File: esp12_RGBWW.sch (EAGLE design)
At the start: 21 parts

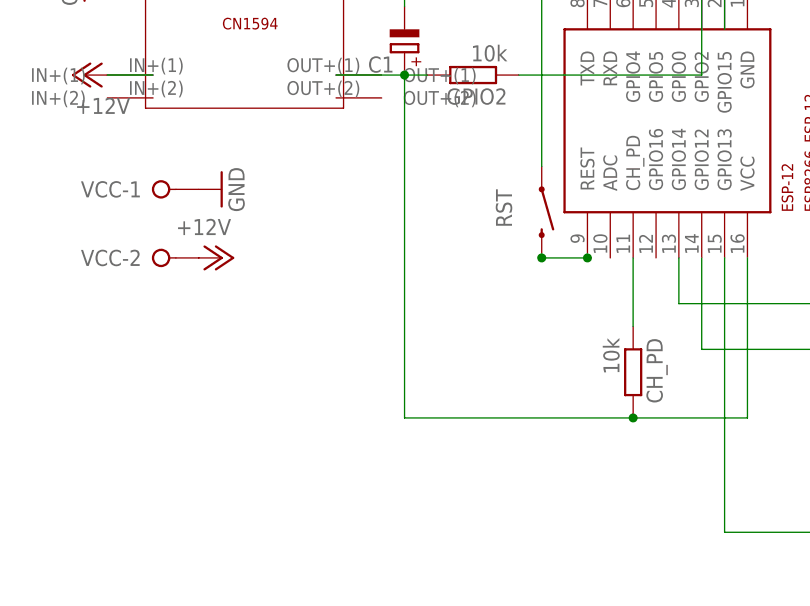
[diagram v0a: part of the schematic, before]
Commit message: added ADC and updated board layout
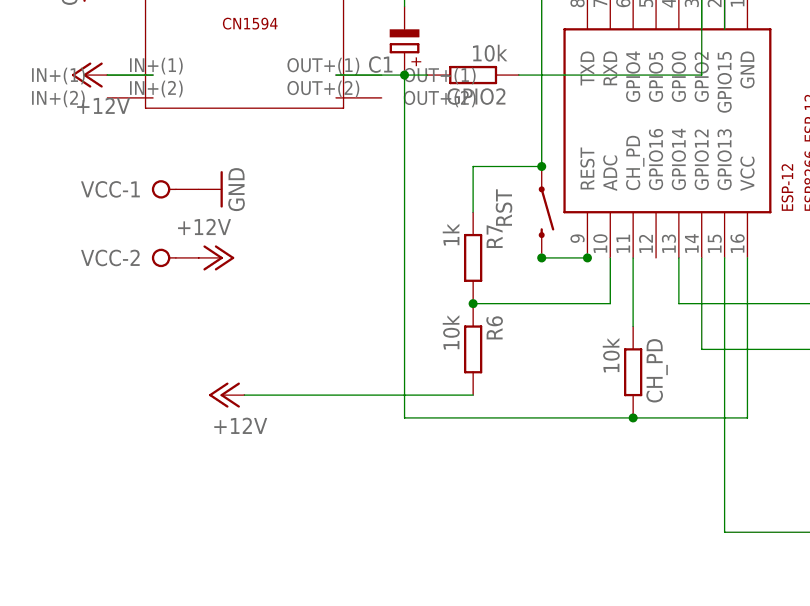
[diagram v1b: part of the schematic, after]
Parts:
- added R6: 10k, rcl:R-EU_R0805
- added R7: 1k, rcl:R-EU_R0805
- CH_PD, GPIO15, GPIO2, R1, R2, R3, R4, R5: device rcl:R-EU_R0603 -> rcl:R-EU_R0805
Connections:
- new net N$21: ESP-12.ADC, R6.1, R7.2
- net +12V: now also R6.2
- net GND3.3V: now also R7.1
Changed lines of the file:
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@@
 <class number="0" name="default" width="0" drill="0">
 </class>
-<class number="1" name="12V" width="1.016" drill="0">
-</class>
-<class number="2" name="GNDRGB" width="1.016" drill="0">
-</class>
-<class number="3" name="3.3V" width="0.635" drill="0">
-</class>
-<class number="4" name="GND3.3V" width="0.635" drill="0">
+<class number="1" name="12V" width="0.508" drill="0">
+</class>
+<class number="2" name="GNDRGB" width="0.508" drill="0">
+</class>
+<class number="3" name="3.3V" width="0.508" drill="0">
+</class>
+<class number="4" name="GND3.3V" width="0.508" drill="0">
 </class>
 <class number="5" name="Signal" width="0.381" drill="0">
@@
 </classes>
 <parts>
-<part name="GPIO2" library="rcl" deviceset="R-EU_" device="R0603" value="10k"/>
-<part name="GPIO15" library="rcl" deviceset="R-EU_" device="R0603" value="10k"/>
-<part name="CH_PD" library="rcl" deviceset="R-EU_" device="R0603" value="10k"/>
+<part name="GPIO2" library="rcl" deviceset="R-EU_" device="R0805" value="10k"/>
+<part name="GPIO15" library="rcl" deviceset="R-EU_" device="R0805" value="10k"/>
+<part name="CH_PD" library="rcl" deviceset="R-EU_" device="R0805" value="10k"/>
 <part name="DC_CONVERTER" library="CN1594_smd" deviceset="CN1594" device="THROUGH-HOLE"/>
 <part name="ESP-12" library="ESP8266-ESP12" deviceset="ESP8266_ESP-12" device=""/>
-<part name="R1" library="rcl" deviceset="R-EU_" device="R0603" value="10k"/>
-<part name="R3" library="rcl" deviceset="R-EU_" device="R0603" value="10k"/>
-<part name="R2" library="rcl" deviceset="R-EU_" device="R0603" value="10k"/>
+<part name="R1" library="rcl" deviceset="R-EU_" device="R0805" value="10k"/>
+<part name="R3" library="rcl" deviceset="R-EU_" device="R0805" value="10k"/>
+<part name="R2" library="rcl" deviceset="R-EU_" device="R0805" value="10k"/>
 <part name="IRLZ44N-WW" library="PAsystem" deviceset="TIP121" device="" value=""/>
 <part name="IRLZ44N-CW" library="PAsystem" deviceset="TIP121" device="" value=""/>
@@
 <part name="IRLZ44N-G" library="PAsystem" deviceset="TIP121" device="" value=""/>
 <part name="IRLZ44N-R" library="PAsystem" deviceset="TIP121" device="" value=""/>
-<part name="R4" library="rcl" deviceset="R-EU_" device="R0603" value="10k"/>
-<part name="R5" library="rcl" deviceset="R-EU_" device="R0603" value="10k"/>
+<part name="R4" library="rcl" deviceset="R-EU_" device="R0805" value="10k"/>
+<part name="R5" library="rcl" deviceset="R-EU_" device="R0805" value="10k"/>
 <part name="P+1" library="supply1" deviceset="+12V" device=""/>
 <part name="P+2" library="supply1" deviceset="+12V" device=""/>
@@
 <part name="RGB" library="con-wago-508" deviceset="W237-04P" device=""/>
 <part name="C1" library="rcl" deviceset="CPOL-EU" device="E3.5-8"/>
+<part name="P+5" library="supply1" deviceset="+12V" device=""/>
+<part name="R6" library="rcl" deviceset="R-EU_" device="R0805" value="10k"/>
+<part name="R7" library="rcl" deviceset="R-EU_" device="R0805" value="1k"/>
 </parts>
 <sheets>
@@
 <instance part="RGB" gate="-4" x="63.5" y="20.32" rot="R180"/>
 <instance part="C1" gate="G$1" x="-48.26" y="53.34" rot="R180"/>
+<instance part="P+5" gate="1" x="-68.58" y="15.24" rot="R90"/>
+<instance part="R6" gate="G$1" x="-40.64" y="20.32" rot="R270"/>
+<instance part="R7" gate="G$1" x="-40.64" y="30.48" rot="R270"/>
 </instances>
 <busses>
@@
 </segment>
 </net>
-<net name="GND" class="2">
+<net name="GND" class="0">
 <segment>
 <pinref part="IRLZ44N-WW" gate="G$1" pin="E"/>
@@
 </segment>
 </net>
-<net name="N$11" class="2">
+<net name="N$11" class="0">
 <segment>
 <pinref part="IRLZ44N-B" gate="G$1" pin="C"/>
@@
 <junction x="-48.26" y="60.96"/>
 <junction x="-10.16" y="76.2"/>
+<wire x1="-40.64" y1="40.64" x2="-33.02" y2="40.64" width="0.1524" layer="91"/>
+<junction x="-33.02" y="40.64"/>
+<pinref part="R7" gate="G$1" pin="1"/>
+<wire x1="-40.64" y1="35.56" x2="-40.64" y2="40.64" width="0.1524" layer="91"/>
 </segment>
 </net>
@@
 <wire x1="-45.72" y1="50.8" x2="-48.26" y2="50.8" width="0.1524" layer="91"/>
 <wire x1="-48.26" y1="50.8" x2="-48.26" y2="12.7" width="0.1524" layer="91"/>
+<junction x="-22.86" y="12.7"/>
 <wire x1="-48.26" y1="12.7" x2="-22.86" y2="12.7" width="0.1524" layer="91"/>
-<junction x="-22.86" y="12.7"/>
 <wire x1="-22.86" y1="12.7" x2="-10.16" y2="12.7" width="0.1524" layer="91"/>
 <wire x1="-55.88" y1="50.8" x2="-48.26" y2="50.8" width="0.1524" layer="91"/>
@@
 <wire x1="-81.28" y1="50.8" x2="-76.2" y2="50.8" width="0.1524" layer="91"/>
 </segment>
+<segment>
+<pinref part="R6" gate="G$1" pin="2"/>
+<pinref part="P+5" gate="1" pin="+12V"/>
+<wire x1="-66.04" y1="15.24" x2="-40.64" y2="15.24" width="0.1524" layer="91"/>
+</segment>
 </net>
 <net name="N$10" class="0">
@@
 </segment>
 </net>
+<net name="N$21" class="4">
+<segment>
+<pinref part="ESP-12" gate="G$1" pin="ADC"/>
+<pinref part="R6" gate="G$1" pin="1"/>
+<wire x1="-40.64" y1="25.4" x2="-25.4" y2="25.4" width="0.1524" layer="91"/>
+<wire x1="-25.4" y1="25.4" x2="-25.4" y2="30.48" width="0.1524" layer="91"/>
+<pinref part="R7" gate="G$1" pin="2"/>
+<junction x="-40.64" y="25.4"/>
+</segment>
+</net>

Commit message: v1.2
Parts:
- added C2: 100n, rcl:C-EUC0805
- added C3: (no value), resistor:CPOL-EUE2.5-6
- added REST: 10k, rcl:R-EU_R0805
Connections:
- removed net GND3.3V: C1.-, DC_CONVERTER.OUT-(2), ESP-12.GND, GPIO15.2, PROG.4, R1.1, R2.2, R3.2, R4.2, R5.2, R7.1, RST.1
- removed net N$20: C1.+, CH_PD.2, DC_CONVERTER.OUT+(1), ESP-12.VCC, GPIO2.2
- new net +3V3: C1.+, C2.2, CH_PD.2, DC_CONVERTER.OUT+(1), ESP-12.VCC, GPIO2.2, REST.1
- net +12V: now also C3.+
- net GND: now also C1.-, C2.1, C3.-, DC_CONVERTER.OUT-(2), ESP-12.GND, GPIO15.2, PROG.4, R1.1, R2.2, R3.2, R4.2, R5.2, R7.1, RST.1
- net N$12: now also REST.2
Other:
- moved on the sheet: C1, CH_PD, GPIO15, GPIO2, IRLZ44N-B, IRLZ44N-CW, IRLZ44N-G, IRLZ44N-R, IRLZ44N-WW, PROG, R1, R2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

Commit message: MOSFET netclass renamed
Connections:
- net N$10 renamed RGB-CW-OUT
- net N$11 renamed RGB-B-OUT
- net N$13 renamed RGB-B
- net N$15 renamed RGB-R-OUT
- net N$23 renamed RGB-R
- net N$24 renamed RGB-CW
- net N$25 renamed RGB-WW
- net N$4 renamed RGB-WW-OUT
- net N$6 renamed RGB-G-OUT
- net R4 renamed RGB-G
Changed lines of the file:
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@@
 </segment>
 </net>
-<net name="N$11" class="0">
+<net name="RGB-B-OUT" class="0">
 <segment>
 <pinref part="IRLZ44N-B" gate="G$1" pin="C"/>
@@
 </segment>
 </net>
-<net name="N$13" class="0">
+<net name="RGB-B" class="0">
 <segment>
 <wire x1="10.16" y1="15.24" x2="10.16" y2="0" width="0.1524" layer="91"/>
@@
 </segment>
 </net>
-<net name="R4" class="0">
+<net name="RGB-G" class="0">
 <segment>
 <wire x1="40.64" y1="20.32" x2="17.78" y2="20.32" width="0.1524" layer="91"/>
@@
 </segment>
 </net>
-<net name="N$15" class="0">
+<net name="RGB-R-OUT" class="0">
 <segment>
 <pinref part="IRLZ44N-R" gate="G$1" pin="C"/>
@@
 </segment>
 </net>
-<net name="N$10" class="0">
+<net name="RGB-CW-OUT" class="0">
 <segment>
 <pinref part="IRLZ44N-CW" gate="G$1" pin="C"/>
@@
 </segment>
 </net>
-<net name="N$6" class="0">
+<net name="RGB-G-OUT" class="0">
 <segment>
 <pinref part="RGB" gate="-3" pin="KL"/>
@@
 </segment>
 </net>
-<net name="N$4" class="0">
+<net name="RGB-WW-OUT" class="0">
 <segment>
 <pinref part="W" gate="-3" pin="KL"/>
@@
 </segment>
 </net>
-<net name="N$23" class="0">
+<net name="RGB-R" class="0">
 <segment>
 <pinref part="ESP-12" gate="G$1" pin="GPIO13"/>
@@
 </segment>
 </net>
-<net name="N$24" class="0">
+<net name="RGB-CW" class="0">
 <segment>
 <pinref part="ESP-12" gate="G$1" pin="GPIO5"/>
@@
 </segment>
 </net>
-<net name="N$25" class="5">
+<net name="RGB-WW" class="5">
 <segment>
 <pinref part="ESP-12" gate="G$1" pin="GPIO4"/>

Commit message: v1.3
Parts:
- added CLR: SWITCH-MOMENTARY-2SMD-1101NE, SparkFun-Electromechanical:SWITCH-MOMENTARY-2SMD-1101NE
- added R8: 10k, rcl:R-EU_R0805
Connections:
- new net N$1: CLR.2, ESP-12.GPIO16, R8.2
- net +3V3: now also R8.1
- net GND: now also CLR.1
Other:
- moved on the sheet: R6, R7, REST, RST

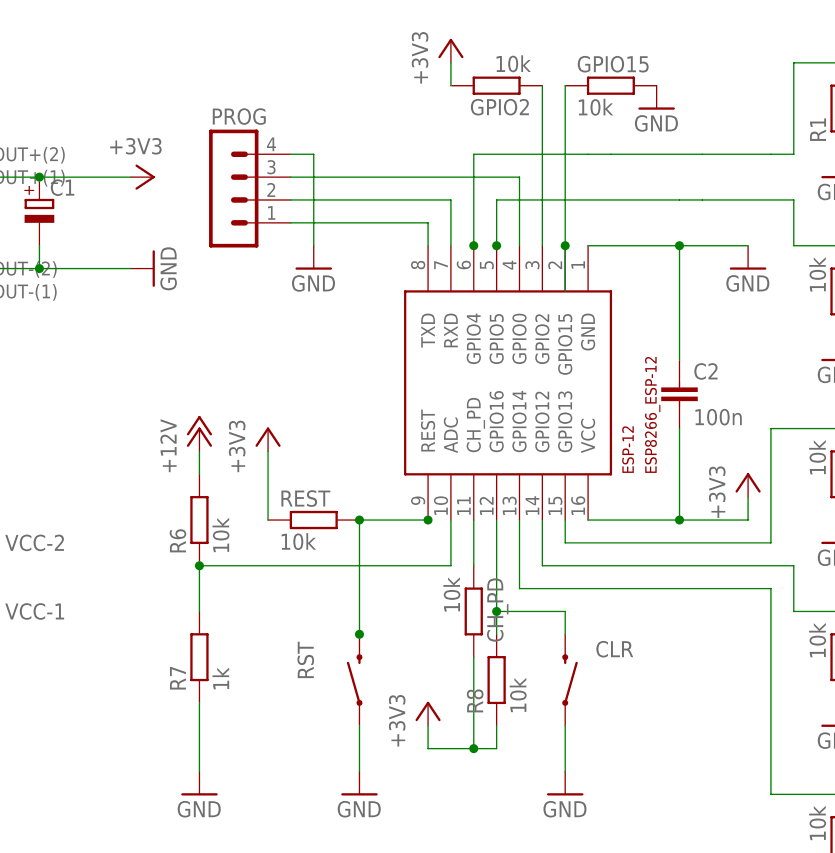
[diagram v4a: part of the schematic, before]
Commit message: updated silkscreen
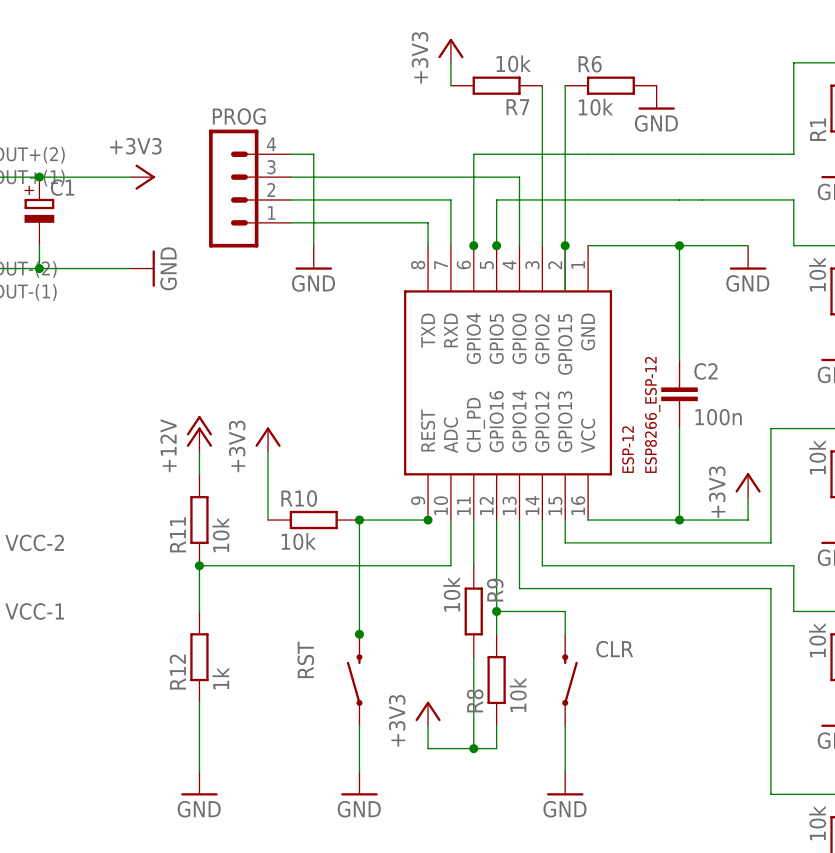
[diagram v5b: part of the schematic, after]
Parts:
- removed GPIO15, GPIO2: 10k, rcl:R-EU_R0805
- added R11: 10k, rcl:R-EU_R0805
- added R12: 1k, rcl:R-EU_R0805
- R7: value 1k -> 10k
- renumbered CH_PD to R9, REST to R10
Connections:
- net +12V: now also R11.2; no longer R6.2
- net +3V3: now also R7.2; no longer GPIO2.2
- net GND: now also R12.1, R6.2; no longer GPIO15.2, R7.1
- net N$21: now also R11.1, R12.2; no longer R6.1, R7.2
- net N$3: now also R7.1; no longer GPIO2.1
- net N$7: now also R6.1; no longer GPIO15.1
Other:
- moved on the sheet: R6, R7
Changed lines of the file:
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@@
 </classes>
 <parts>
-<part name="GPIO2" library="rcl" deviceset="R-EU_" device="R0805" value="10k"/>
-<part name="GPIO15" library="rcl" deviceset="R-EU_" device="R0805" value="10k"/>
-<part name="CH_PD" library="rcl" deviceset="R-EU_" device="R0805" value="10k"/>
+<part name="R7" library="rcl" deviceset="R-EU_" device="R0805" value="10k"/>
+<part name="R6" library="rcl" deviceset="R-EU_" device="R0805" value="10k"/>
+<part name="R9" library="rcl" deviceset="R-EU_" device="R0805" value="10k"/>
 <part name="DC_CONVERTER" library="CN1594_smd" deviceset="CN1594" device="THROUGH-HOLE"/>
 <part name="ESP-12" library="ESP8266-ESP12" deviceset="ESP8266_ESP-12" device=""/>
@@
 <part name="C1" library="rcl" deviceset="CPOL-EU" device="E3.5-8"/>
 <part name="P+5" library="supply1" deviceset="+12V" device=""/>
-<part name="R6" library="rcl" deviceset="R-EU_" device="R0805" value="10k"/>
-<part name="R7" library="rcl" deviceset="R-EU_" device="R0805" value="1k"/>
+<part name="R11" library="rcl" deviceset="R-EU_" device="R0805" value="10k"/>
+<part name="R12" library="rcl" deviceset="R-EU_" device="R0805" value="1k"/>
 <part name="+3V1" library="supply1" deviceset="+3V3" device=""/>
 <part name="+3V2" library="supply1" deviceset="+3V3" device=""/>
@@
 <part name="+3V4" library="supply1" deviceset="+3V3" device=""/>
 <part name="GND13" library="supply1" deviceset="GND" device=""/>
-<part name="REST" library="rcl" deviceset="R-EU_" device="R0805" value="10k"/>
+<part name="R10" library="rcl" deviceset="R-EU_" device="R0805" value="10k"/>
 <part name="+3V5" library="supply1" deviceset="+3V3" device=""/>
 <part name="C2" library="rcl" deviceset="C-EU" device="C0805" value="100n"/>
@@
 </plain>
 <instances>
-<instance part="GPIO2" gate="G$1" x="-20.32" y="78.74" rot="R180"/>
-<instance part="GPIO15" gate="G$1" x="-7.62" y="78.74"/>
-<instance part="CH_PD" gate="G$1" x="-22.86" y="20.32" rot="R270"/>
+<instance part="R7" gate="G$1" x="-20.32" y="78.74" rot="R180"/>
+<instance part="R6" gate="G$1" x="-7.62" y="78.74"/>
+<instance part="R9" gate="G$1" x="-22.86" y="20.32" rot="R270"/>
 <instance part="DC_CONVERTER" gate="G$1" x="-93.98" y="63.5" smashed="yes" rot="MR180"/>
 <instance part="ESP-12" gate="G$1" x="-20.32" y="53.34" rot="R90"/>
@@
 <instance part="C1" gate="G$1" x="-71.12" y="66.04"/>
 <instance part="P+5" gate="1" x="-53.34" y="40.64"/>
-<instance part="R6" gate="G$1" x="-53.34" y="30.48" rot="R90"/>
-<instance part="R7" gate="G$1" x="-53.34" y="15.24" rot="R90"/>
+<instance part="R11" gate="G$1" x="-53.34" y="30.48" rot="R90"/>
+<instance part="R12" gate="G$1" x="-53.34" y="15.24" rot="R90"/>
 <instance part="+3V1" gate="G$1" x="-58.42" y="68.58" rot="R270"/>
 <instance part="+3V2" gate="G$1" x="7.62" y="35.56"/>
@@
 <instance part="+3V4" gate="G$1" x="-27.94" y="10.16"/>
 <instance part="GND13" gate="1" x="-40.64" y="58.42"/>
-<instance part="REST" gate="G$1" x="-40.64" y="30.48"/>
+<instance part="R10" gate="G$1" x="-40.64" y="30.48"/>
 <instance part="+3V5" gate="G$1" x="-45.72" y="40.64"/>
 <instance part="C2" gate="G$1" x="0" y="45.72"/>
@@
 <net name="N$2" class="5">
 <segment>
-<pinref part="CH_PD" gate="G$1" pin="1"/>
+<pinref part="R9" gate="G$1" pin="1"/>
 <wire x1="-22.86" y1="30.48" x2="-22.86" y2="25.4" width="0.1524" layer="91"/>
 <pinref part="ESP-12" gate="G$1" pin="CH_PD"/>
@@
 <net name="N$3" class="0">
 <segment>
-<pinref part="GPIO2" gate="G$1" pin="1"/>
+<pinref part="R7" gate="G$1" pin="1"/>
 <pinref part="ESP-12" gate="G$1" pin="GPIO2"/>
 <wire x1="-15.24" y1="60.96" x2="-15.24" y2="78.74" width="0.1524" layer="91"/>
@@
 </segment>
 <segment>
-<pinref part="R7" gate="G$1" pin="1"/>
+<pinref part="R12" gate="G$1" pin="1"/>
 <pinref part="GND5" gate="1" pin="GND"/>
 <wire x1="-53.34" y1="10.16" x2="-53.34" y2="2.54" width="0.1524" layer="91"/>
@@
 </segment>
 <segment>
-<pinref part="GPIO15" gate="G$1" pin="2"/>
+<pinref part="R6" gate="G$1" pin="2"/>
 <pinref part="GND12" gate="1" pin="GND"/>
 </segment>
@@
 <junction x="-27.94" y="30.48"/>
 <wire x1="-35.56" y1="17.78" x2="-35.56" y2="30.48" width="0.1524" layer="91"/>
-<pinref part="REST" gate="G$1" pin="2"/>
+<pinref part="R10" gate="G$1" pin="2"/>
 <wire x1="-35.56" y1="30.48" x2="-27.94" y2="30.48" width="0.1524" layer="91"/>
 <junction x="-35.56" y="30.48"/>
@@
 <net name="N$7" class="0">
 <segment>
-<pinref part="GPIO15" gate="G$1" pin="1"/>
+<pinref part="R6" gate="G$1" pin="1"/>
 <wire x1="-12.7" y1="78.74" x2="-12.7" y2="60.96" width="0.1524" layer="91"/>
 <pinref part="ESP-12" gate="G$1" pin="GPIO15"/>
@@
 </segment>
 <segment>
-<pinref part="R6" gate="G$1" pin="2"/>
+<pinref part="R11" gate="G$1" pin="2"/>
 <pinref part="P+5" gate="1" pin="+12V"/>
 <wire x1="-53.34" y1="38.1" x2="-53.34" y2="35.56" width="0.1524" layer="91"/>
@@
 <segment>
 <pinref part="ESP-12" gate="G$1" pin="ADC"/>
-<pinref part="R6" gate="G$1" pin="1"/>
+<pinref part="R11" gate="G$1" pin="1"/>
 <wire x1="-53.34" y1="25.4" x2="-25.4" y2="25.4" width="0.1524" layer="91"/>
 <wire x1="-25.4" y1="25.4" x2="-25.4" y2="30.48" width="0.1524" layer="91"/>
-<pinref part="R7" gate="G$1" pin="2"/>
+<pinref part="R12" gate="G$1" pin="2"/>
 <junction x="-53.34" y="25.4"/>
 <wire x1="-53.34" y1="25.4" x2="-53.34" y2="20.32" width="0.1524" layer="91"/>
@@
 </segment>
 <segment>
-<pinref part="GPIO2" gate="G$1" pin="2"/>
+<pinref part="R7" gate="G$1" pin="2"/>
 <pinref part="+3V3" gate="G$1" pin="+3V3"/>
 <wire x1="-25.4" y1="78.74" x2="-25.4" y2="81.28" width="0.1524" layer="91"/>
 </segment>
 <segment>
-<pinref part="CH_PD" gate="G$1" pin="2"/>
+<pinref part="R9" gate="G$1" pin="2"/>
 <wire x1="-27.94" y1="7.62" x2="-27.94" y2="5.08" width="0.1524" layer="91"/>
 <wire x1="-27.94" y1="5.08" x2="-22.86" y2="5.08" width="0.1524" layer="91"/>
@@
 </segment>
 <segment>
-<pinref part="REST" gate="G$1" pin="1"/>
+<pinref part="R10" gate="G$1" pin="1"/>
 <pinref part="+3V5" gate="G$1" pin="+3V3"/>
 <wire x1="-45.72" y1="30.48" x2="-45.72" y2="38.1" width="0.1524" layer="91"/>

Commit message: updated schematics and board v1.5
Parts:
- removed DC_CONVERTER: CN1594THROUGH-HOLE, CN1594_smd:CN1594THROUGH-HOLE
- removed R11: 10k, rcl:R-EU_R0805
- removed R12: 1k, rcl:R-EU_R0805
- added CLR1, RST1: SWITCH-MOMENTARY-2SMD-1101NE, SparkFun-Electromechanical:SWITCH-MOMENTARY-2SMD-1101NE
- added SV1: (no value), con-lstb:MA03-1
- added U$2: XM1584, XM1584:XM1584
- C1: device rcl:CPOL-EUE3.5-8 -> resistor:CPOL-EUE2.5-6
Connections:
- removed net N$21: ESP-12.ADC, R11.1, R12.2
- new net DCDC+: SV1.1, U$2.OUT+(1), U$2.OUT+(2)
- net +12V: now also U$2.IN+(1), U$2.IN+(2); no longer DC_CONVERTER.IN+(1), R11.2
- net +3V3: now also SV1.2; no longer DC_CONVERTER.OUT+(1)
- net GND: now also CLR1.1, RST1.1, SV1.3, U$2.IN-(1), U$2.IN-(2), U$2.OUT-(1), U$2.OUT-(2); no longer DC_CONVERTER.IN-(2), DC_CONVERTER.OUT-(2), R12.1
- net N$1: now also CLR1.2
- net N$12: now also RST1.2
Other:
- moved on the sheet: C1, C2, VCC-1, VCC-2
